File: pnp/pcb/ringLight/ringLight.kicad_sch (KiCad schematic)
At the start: 14 parts, among them J1 Conn_01x03_Male, J2 Conn_01x03_Male

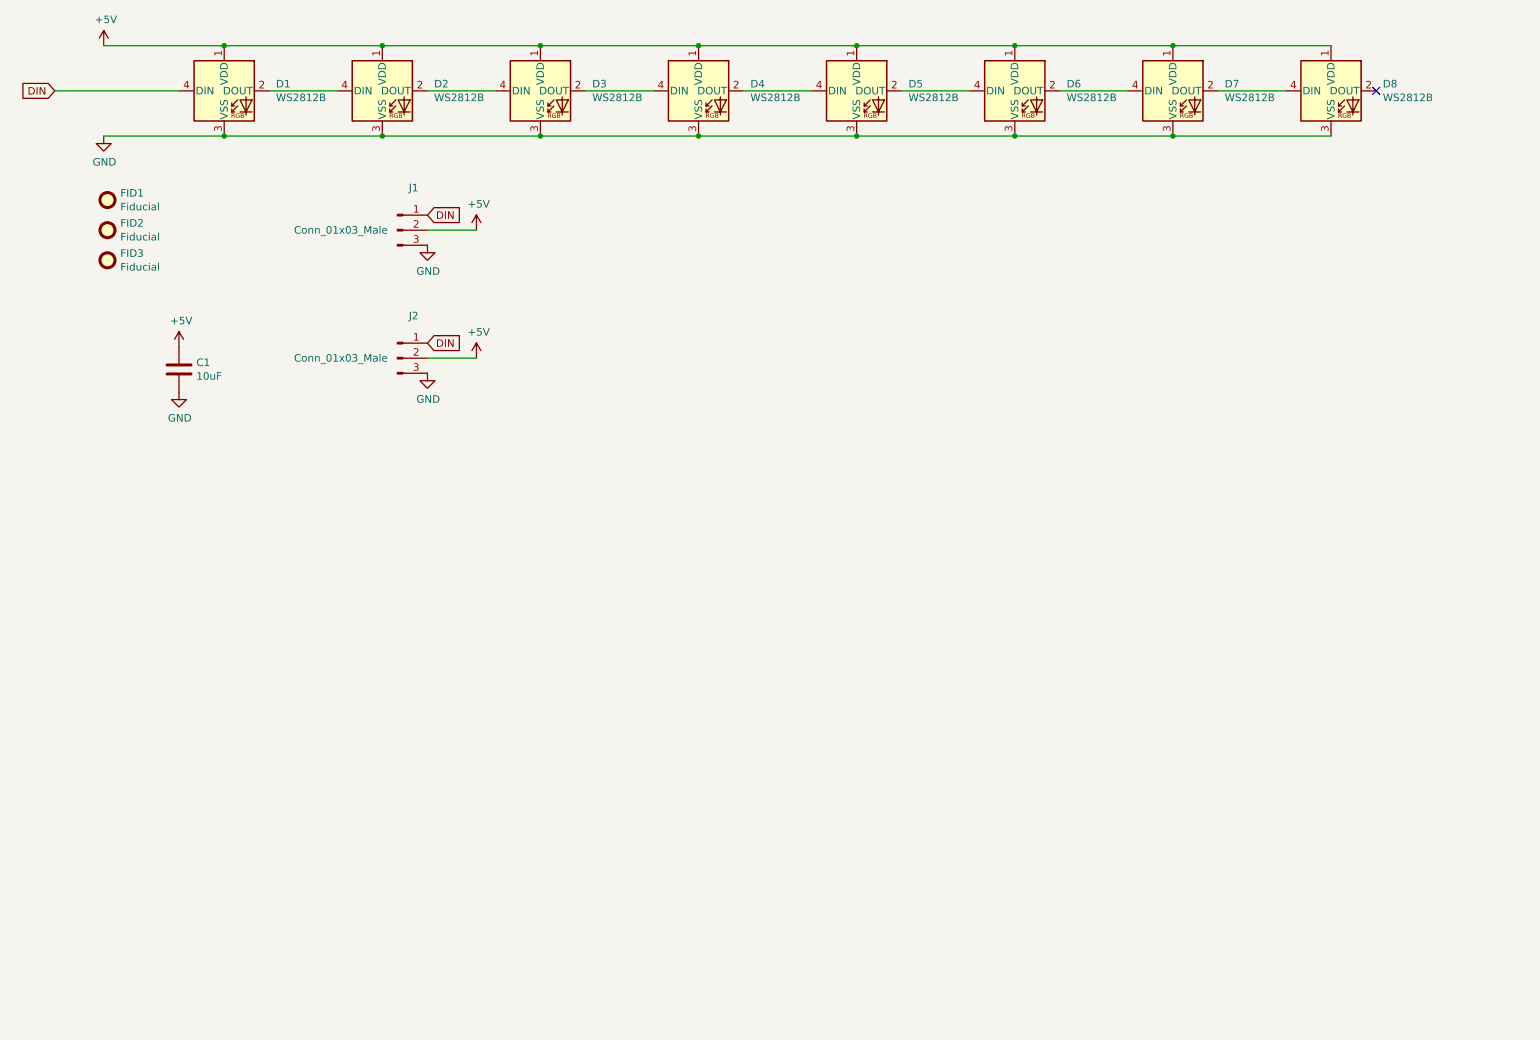
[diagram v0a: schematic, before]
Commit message: cleaned up routing, standardized capacitor values based on datasheet recommendation for OR gate, picked more readily available footprint for OR gate, rearranged part identifiers on silkscreen
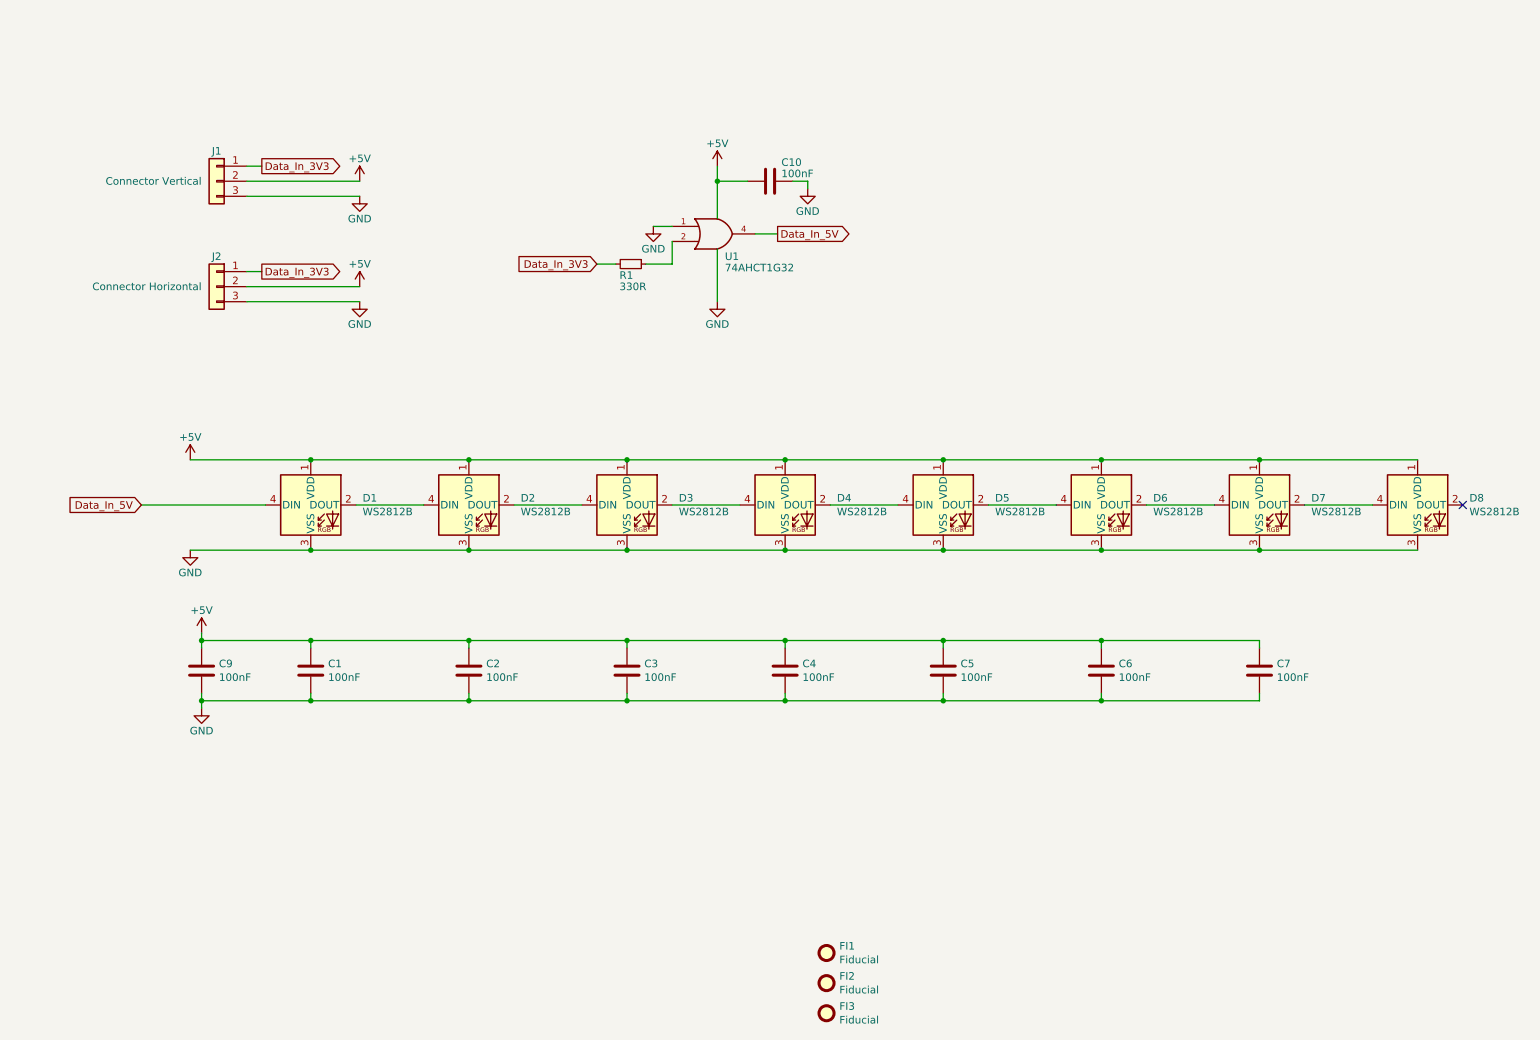
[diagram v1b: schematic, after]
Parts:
- removed J1: Conn_01x03_Male, Connector_JST:JST_XH_B3B-XH-A_1x03_P2.50mm_Vertical, symbol Connector:Conn_01x03_Male
- removed J2: Conn_01x03_Male, index:S3B-XH-SM4-TB, symbol Connector:Conn_01x03_Male
- added C10, C2, C3, C4, C5, C6, C7, C9: 100nF, Capacitor_SMD:C_0805_2012Metric, symbol Device:C
- added J1: Connector Vertical, Connector_JST:JST_XH_B3B-XH-A_1x03_P2.50mm_Vertical, symbol Connector_Generic:Conn_01x03
- added J2: Connector Horizontal, Connector_JST:JST_XH_S3B-XH-A-1_1x03_P2.50mm_Horizontal, symbol Connector_Generic:Conn_01x03
- added R1: 330R, Resistor_SMD:R_0805_2012Metric, symbol Device:R_Small
- added U1: 74AHCT1G32, Package_TO_SOT_SMD:SOT-353_SC-70-5, symbol 74xGxx:74AHCT1G32
- C1: value 10uF -> 100nF; JLCPCB (none) -> C49678; LCSC (none) -> C49678; Part # (none) -> CC0805KRX7R9BB104
- D1, D2, D3, D4, D5, D6, D7, D8: Part # (none) -> WS2812B
- renumbered FID1 to FI1, FID2 to FI2, FID3 to FI3
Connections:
- net +5V: now also C10.1, C2.1, C3.1, C4.1, C5.1, C6.1, C7.1, C9.1, J1.2 (Pin_2), J2.2 (Pin_2), U1.5 (VCC)
- net GND: now also C10.2, C2.2, C3.2, C4.2, C5.2, C6.2, C7.2, C9.2, J1.3 (Pin_3), J2.3 (Pin_3), U1.1, U1.3 (GND)
- net DIN renamed Data_In_5V
- net Data_In_5V: now also U1.4
- new net: R1.1, U1.2
- new net Data_In_3V3: J1.1 (Pin_1), J2.1 (Pin_1), R1.2
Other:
- title: (none) -> Index - Ring Light
- moved on the sheet: D1, D2, D3, D4, D5, D6, D7, D8, FI1, FI2, FI3

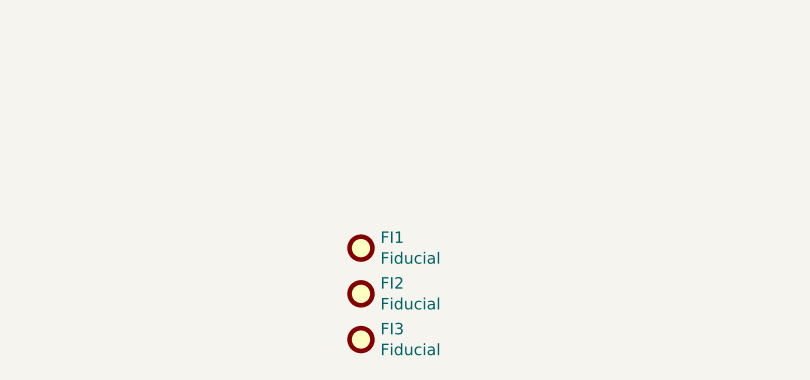
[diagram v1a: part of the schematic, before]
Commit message: Improved ringlight silkscreen
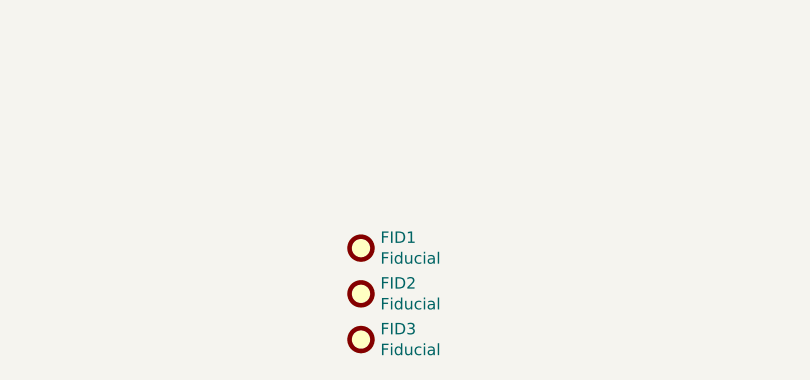
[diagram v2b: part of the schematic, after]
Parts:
- renumbered FI1 to FID1, FI2 to FID2, FI3 to FID3
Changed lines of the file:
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@@
   (symbol (lib_id "Mechanical:Fiducial") (at 153.67 174.625 0) (unit 1)
     (in_bom yes) (on_board yes)
-    (property "Reference" "FI1" (id 0) (at 155.829 173.4566 0)
+    (property "Reference" "FID1" (id 0) (at 155.829 173.4566 0)
       (effects (font (size 1.27 1.27)) (justify left))
     )
@@
   (symbol (lib_id "Mechanical:Fiducial") (at 153.67 179.705 0) (unit 1)
     (in_bom yes) (on_board yes)
-    (property "Reference" "FI2" (id 0) (at 155.829 178.5366 0)
+    (property "Reference" "FID2" (id 0) (at 155.829 178.5366 0)
       (effects (font (size 1.27 1.27)) (justify left))
     )
@@
   (symbol (lib_id "Mechanical:Fiducial") (at 153.67 184.785 0) (unit 1)
     (in_bom yes) (on_board yes)
-    (property "Reference" "FI3" (id 0) (at 155.829 183.6166 0)
+    (property "Reference" "FID3" (id 0) (at 155.829 183.6166 0)
       (effects (font (size 1.27 1.27)) (justify left))
     )
@@
     )
     (path "/00000000-0000-0000-0000-00005ff0d105"
-      (reference "FI1") (unit 1) (value "Fiducial") (footprint "Fiducial:Fiducial_1mm_Mask2mm")
+      (reference "FID1") (unit 1) (value "Fiducial") (footprint "Fiducial:Fiducial_1mm_Mask2mm")
     )
     (path "/00000000-0000-0000-0000-00005ff0e50a"
-      (reference "FI2") (unit 1) (value "Fiducial") (footprint "Fiducial:Fiducial_1mm_Mask2mm")
+      (reference "FID2") (unit 1) (value "Fiducial") (footprint "Fiducial:Fiducial_1mm_Mask2mm")
     )
     (path "/00000000-0000-0000-0000-00005ff0eab4"
-      (reference "FI3") (unit 1) (value "Fiducial") (footprint "Fiducial:Fiducial_1mm_Mask2mm")
+      (reference "FID3") (unit 1) (value "Fiducial") (footprint "Fiducial:Fiducial_1mm_Mask2mm")
     )
     (path "/00000000-0000-0000-0000-00006141224d"
